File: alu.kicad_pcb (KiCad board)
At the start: 2 copper layers, 100 x 100 mm, 50 parts, among them J0 640-USB4970-00-A, Q0 DMG2302U-7, Q1 DMG2302U-7, Q2 DMG2302U-7, Q3 DMG2302U-7, Q4 DMG2302U-7, Q5 DMG2302U-7, SW0 418127270904, SW1 418127270904, SW2 418127270904, U0 SN74LS08N, U1 SN74HC86N, U10 SN74LVC1G32DBVR, U11 SN74LS08N, U12 SN74LS08N, U13 CD74HCT32E, U14 CD74HCT32E, U2 SN74HC86N, U3 SN74LS08N, U4 SN74LS08N, U5 CD74HCT32E, U6 SN74LS08N, U7 SN74LS08N, U8 SN74HC86N, U9 SN74LS08N

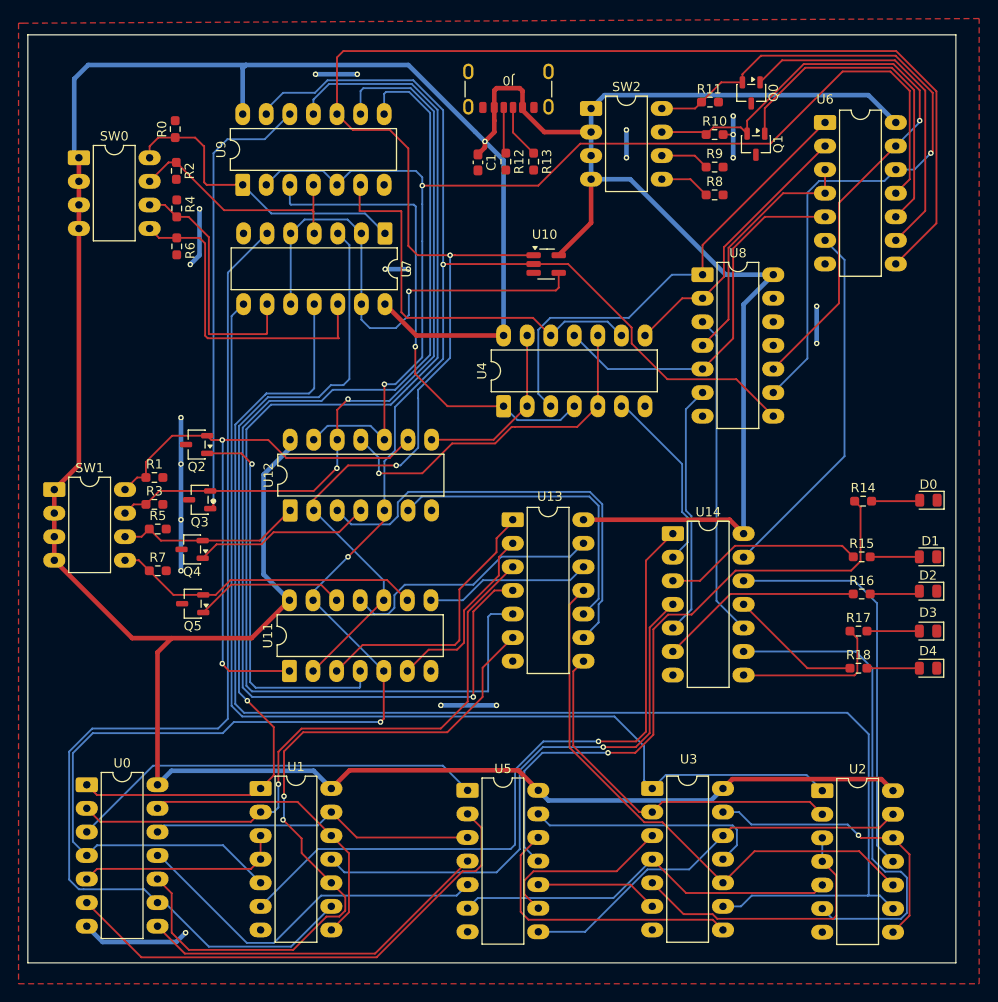
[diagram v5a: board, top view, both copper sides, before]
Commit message: fix: updated pcb with capas
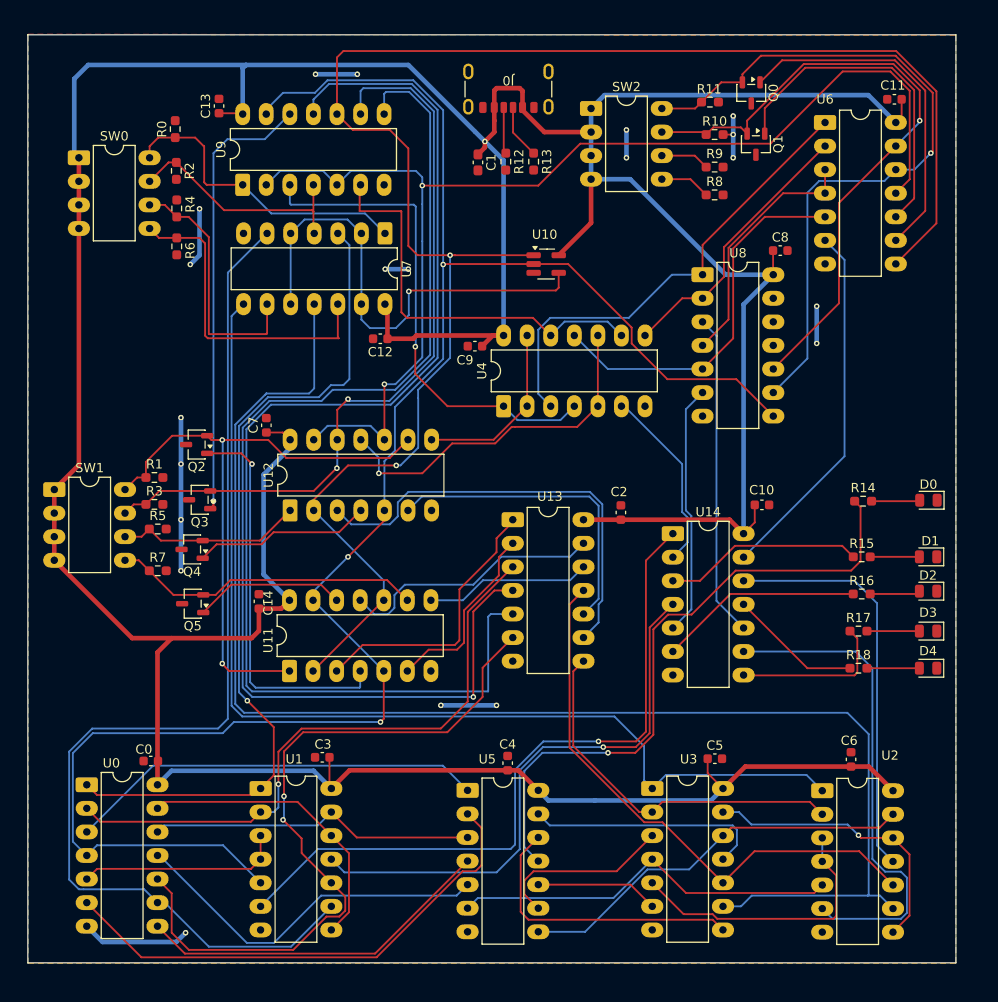
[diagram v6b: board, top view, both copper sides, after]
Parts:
- added C0: C_Small, Capacitor_SMD:C_0603_1608Metric, F.Cu at (66.8, 147.0)
- added C10: C_Small, Capacitor_SMD:C_0603_1608Metric, F.Cu at (132.6, 119.4)
- added C11: C_Small, Capacitor_SMD:C_0603_1608Metric, F.Cu at (146.9, 75.7)
- added C12: C_Small, Capacitor_SMD:C_0603_1608Metric, F.Cu at (91.5, 101.5)
- added C13: C_Small, Capacitor_SMD:C_0603_1608Metric, F.Cu at (74.1, 76.4)
- added C14: C_Small, Capacitor_SMD:C_0603_1608Metric, F.Cu at (78.4, 129.8)
- added C2: C_Small, Capacitor_SMD:C_0603_1608Metric, F.Cu at (117.4, 120.2)
- added C3: C_Small, Capacitor_SMD:C_0603_1608Metric, F.Cu at (85.2, 146.6)
- added C4: C_Small, Capacitor_SMD:C_0603_1608Metric, F.Cu at (105.2, 147.2)
- added C5: C_Small, Capacitor_SMD:C_0603_1608Metric, F.Cu at (127.5, 146.8)
- added C6: C_Small, Capacitor_SMD:C_0603_1608Metric, F.Cu at (142.2, 146.8)
- added C7: C_Small, Capacitor_SMD:C_0603_1608Metric, F.Cu at (79.2, 110.8)
- added C8: C_Small, Capacitor_SMD:C_0603_1608Metric, F.Cu at (134.6, 92.0)
- added C9: C_Small, Capacitor_SMD:C_0603_1608Metric, F.Cu at (101.7, 102.3)
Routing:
- net +5V: track 440.0 -> 470.6 mm

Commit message: feat(pcb): pull up and 1mm 5v and 0 error/warning
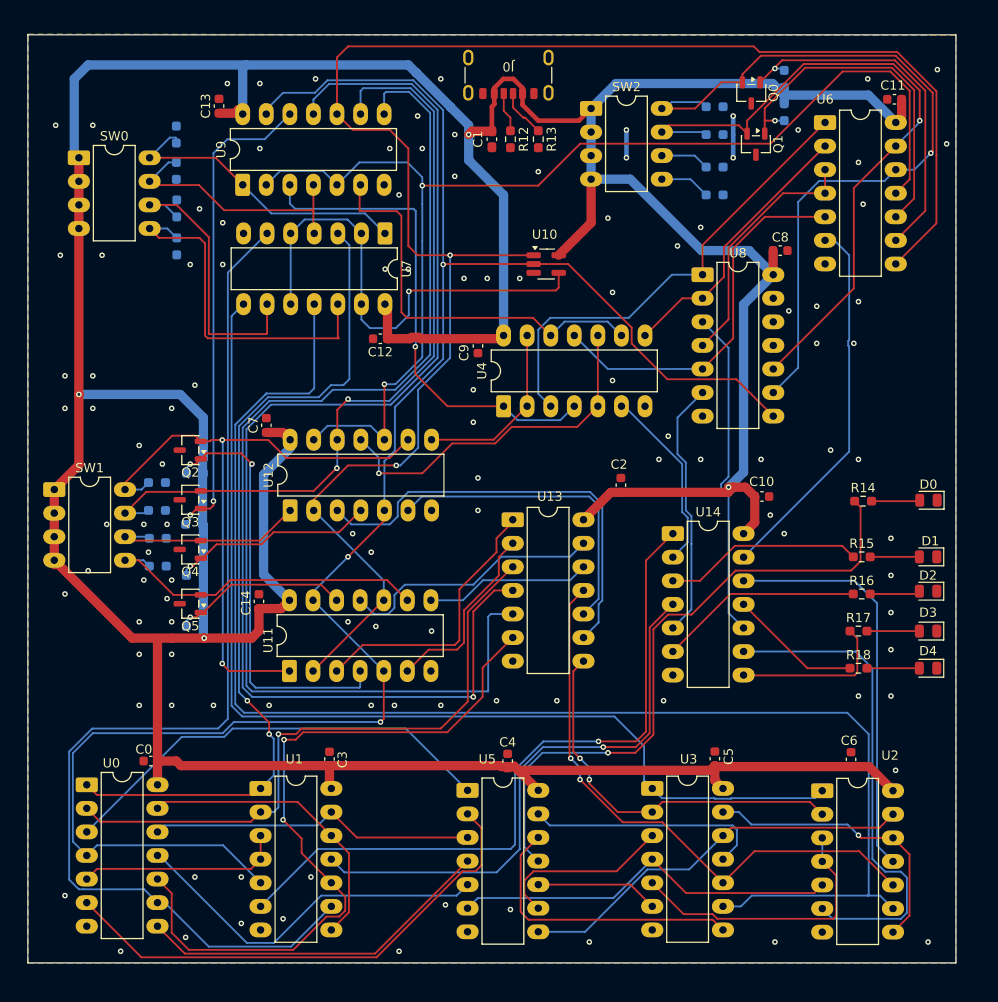
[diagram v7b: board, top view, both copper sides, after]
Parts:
- added R19: 10k, Resistor_SMD:R_0603_1608Metric_Pad0.98x0.95mm_HandSolder, B.Cu at (135.0, 77.1)
- added R20: 10k, Resistor_SMD:R_0603_1608Metric_Pad0.98x0.95mm_HandSolder, B.Cu at (135.0, 73.5)
- added R21: 10k, Resistor_SMD:R_0603_1608Metric_Pad0.98x0.95mm_HandSolder, B.Cu at (71.5, 132.5)
- added R22: 10k, Resistor_SMD:R_0603_1608Metric_Pad0.98x0.95mm_HandSolder, B.Cu at (71.5, 127.0)
- added R23: 10k, Resistor_SMD:R_0603_1608Metric_Pad0.98x0.95mm_HandSolder, B.Cu at (71.4, 121.5)
- added R24: 10k, Resistor_SMD:R_0603_1608Metric_Pad0.98x0.95mm_HandSolder, B.Cu at (71.5, 116.0)
- R0, R1, R10, R11, R2, R3, R4, R5, R6, R7, R8, R9: value CRG0603J10K - 3399584 -> 10k; moved to B.Cu
- moved C2 2.95 mm to (117.4, 117.3)
- moved C1 2.92 mm to (103.5, 80.0)
- moved R12 2.46 mm to (105.5, 80.0)
- moved R13 2.46 mm to (108.5, 80.0)
- moved J0 1.50 mm to (105.3, 72.0)
- moved Q3 1.01 mm to (71.0, 118.8)
- moved R5 1.00 mm to (67.5, 123.0)
- moved Q2 0.91 mm to (71.0, 113.5)
- moved C10 0.90 mm to (132.6, 118.5)
- moved C3 0.79 mm to (86.0, 146.8), turned to 90 degrees
- moved R11 0.71 mm to (127.5, 76.5)
- moved R3 0.71 mm to (67.4, 120.0)
- moved R1 0.61 mm to (67.4, 117.0)
- moved R0 0.60 mm to (69.5, 79.5)
- moved R7 0.50 mm to (67.5, 126.0)
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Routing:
- net GND: track 60.6 -> 7.50 mm, vias 20 -> 114
- net +5V: track 470.6 -> 504.6 mm, vias 1 -> 4
- net /binary-decoder/IN_OP1: track 78.4 -> 83.7 mm
- net /binary-decoder/IN_OP2: track 70.2 -> 75.0 mm
- net Net-(Q3-D): track 48.4 -> 52.1 mm, vias 1 -> 2
- net Net-(Q2-D): track 42.8 -> 46.2 mm, vias 1 -> 2
- net IN_A2: track 27.7 -> 31.2 mm
- net IN_A3: track 34.8 -> 38.2 mm
- net Net-(U0-Pad3): track 45.3 -> 48.6 mm
- net IN_B3: track 33.5 -> 36.4 mm
- net Net-(Q4-D): track 19.2 -> 22.0 mm, vias 0 -> 1
- net Net-(Q5-D): track 16.3 -> 19.1 mm, vias 0 -> 1
- net IN_B1: track 82.1 -> 84.8 mm
- net IN_B0: track 67.9 -> 70.3 mm
- net Net-(Q1-D): track 36.1 -> 38.2 mm, vias 0 -> 1
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- added copper zone on B.Cu, net GND

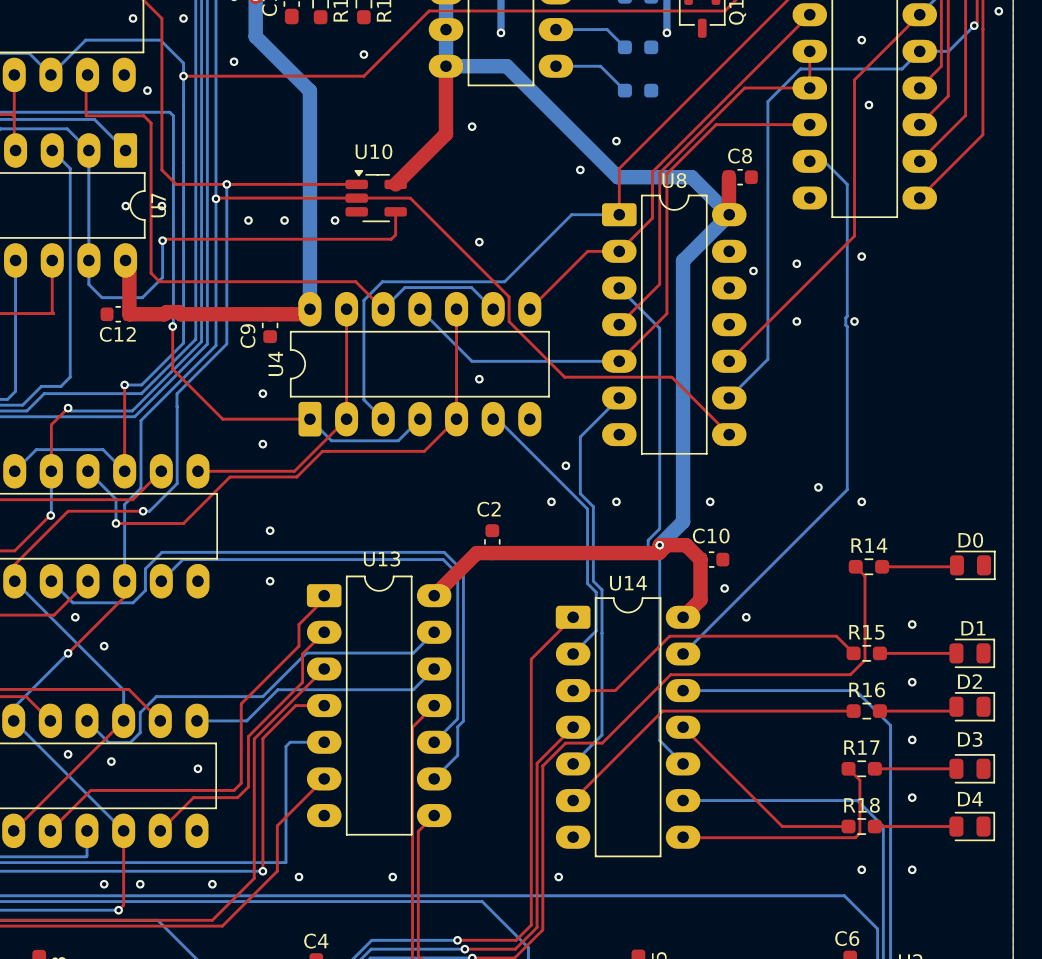
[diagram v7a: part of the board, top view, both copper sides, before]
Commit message: feat: added op led
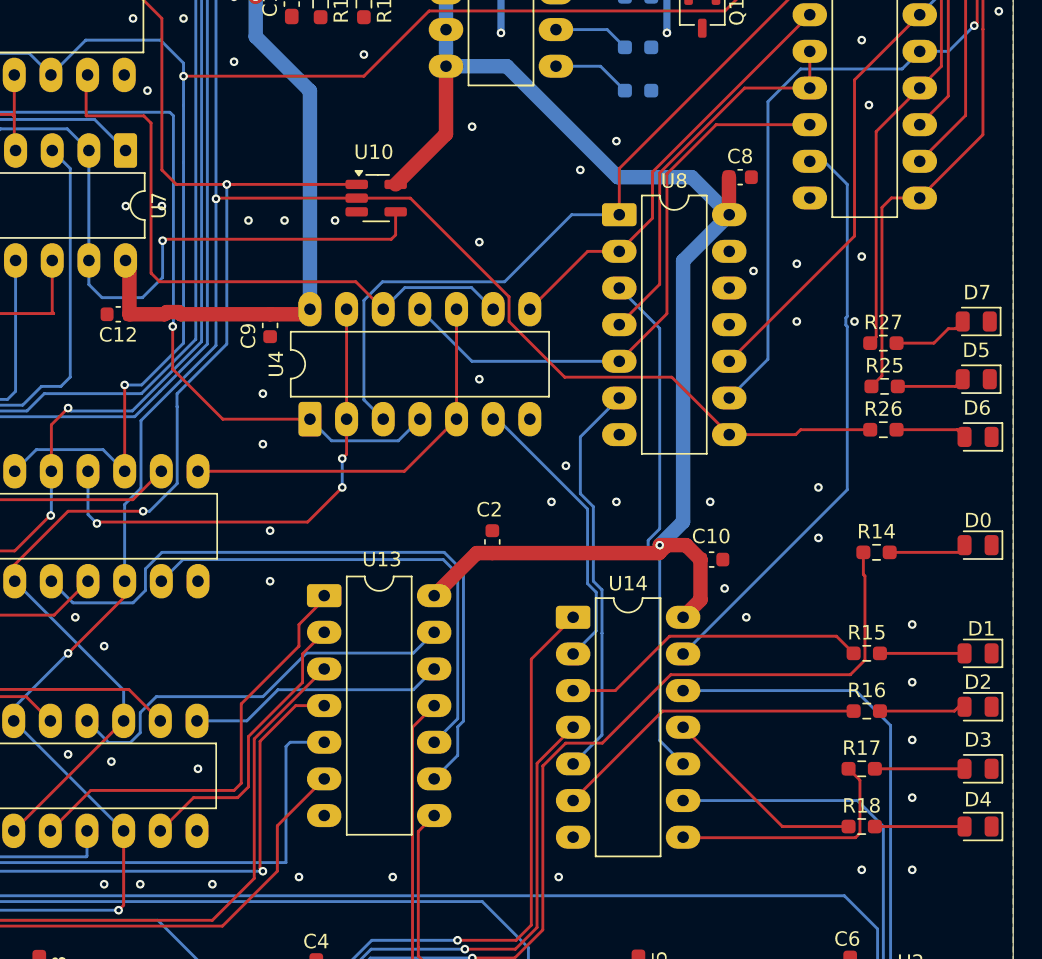
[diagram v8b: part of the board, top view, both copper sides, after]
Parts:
- added D5: 150080RS75000, LED_SMD:LED_0805_2012Metric, F.Cu at (150.9, 106.0)
- added D6: 150080RS75000, LED_SMD:LED_0805_2012Metric, F.Cu at (151.1, 110.0)
- added D7: 150080RS75000, LED_SMD:LED_0805_2012Metric, F.Cu at (150.9, 102.0)
- added R25: RC0603FR-07220RL, Resistor_SMD:R_0603_1608Metric_Pad0.98x0.95mm_HandSolder, F.Cu at (144.6, 106.5)
- added R26: RC0603FR-07220RL, Resistor_SMD:R_0603_1608Metric_Pad0.98x0.95mm_HandSolder, F.Cu at (144.5, 109.5)
- added R27: RC0603FR-07220RL, Resistor_SMD:R_0603_1608Metric_Pad0.98x0.95mm_HandSolder, F.Cu at (144.5, 103.5)
- R0, R1, R10, R11, R2, R3, R4, R5, R6, R7, R8, R9: value 10k -> CRG0603J10K - 3399584
- moved D0 1.50 mm to (151.1, 117.5)
- moved R14 1.13 mm to (144.0, 118.0)
- moved D1 0.56 mm to (151.1, 125.0)
- moved D2 0.56 mm to (151.1, 128.7)
- moved D3 0.56 mm to (151.1, 133.0)
- moved D4 0.56 mm to (151.1, 137.0)
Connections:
- J0 pad S1: (no net) -> GND
- U4 pad 10: OUT_SEL_MUL_B1 -> OUT_SEL_MUL_B0
- U4 pad 13: OUT_SEL_MUL_B0 -> OUT_SEL_MUL_B1
- U4 pad 2: OUT_SEL_MUL_B0 -> OUT_SEL_MUL_B1
- U4 pad 5: OUT_SEL_MUL_B1 -> OUT_SEL_MUL_B0
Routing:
- net MUL: track 129.4 -> 148.5 mm
- net ADD: track 188.2 -> 203.8 mm
- net SUB: track 207.7 -> 217.6 mm
- net OUT_SEL_MUL_B0: track 19.4 -> 27.0 mm
- net Net-(D7-A): track 0.00 -> 5.21 mm
- net Net-(D6-A): track 0.00 -> 4.92 mm
- net Net-(D5-A): track 0.00 -> 4.71 mm
- net OUT_SEL_MUL_B1: track 38.6 -> 34.4 mm, vias 1 -> 3
- net ADD_OVERFLOW: track 69.3 -> 70.1 mm
- net Net-(D4-A): track 5.65 -> 6.21 mm
- net Net-(D3-A): track 5.65 -> 6.21 mm
- net Net-(D1-A): track 5.30 -> 5.86 mm
